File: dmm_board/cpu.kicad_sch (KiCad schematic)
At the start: 3 parts

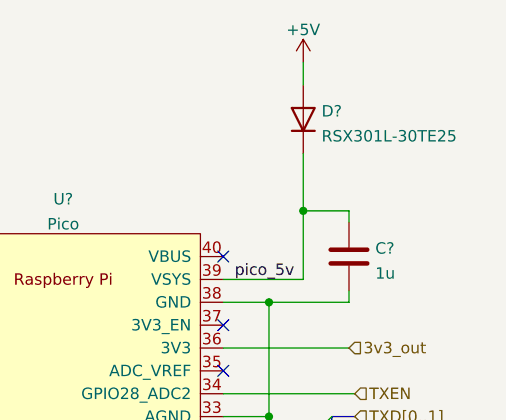
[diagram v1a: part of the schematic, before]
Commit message: more analog input work
need new amp for current -8 instead of -9 that
-8 is unity gain stable -9 is not
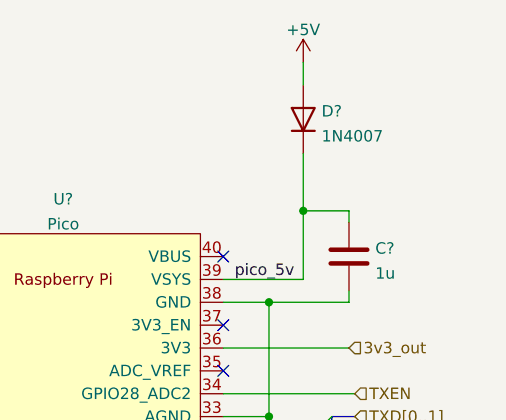
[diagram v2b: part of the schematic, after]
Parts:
- removed D?: RSX301L-30TE25, good_things:SOD-106, symbol Device:D
- added D?: 1N4007, Diode_THT:D_DO-41_SOD81_P7.62mm_Horizontal, symbol Device:D
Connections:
- net +5V: now also D?.2 (A)
- net pico_5v: now also D?.1 (K)
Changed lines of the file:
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@@
       (effects (font (size 1.27 1.27)) (justify right))
     )
-    (property "Value" "RSX301L-30TE25" (id 1) (at 121.412 37.4266 90)
+    (property "Value" "1N4007" (id 1) (at 121.412 37.4266 90)
       (effects (font (size 1.27 1.27)) (justify right))
     )
-    (property "Footprint" "good_things:SOD-106" (id 2) (at 119.38 35.56 0)
+    (property "Footprint" "Diode_THT:D_DO-41_SOD81_P7.62mm_Horizontal" (id 2) (at 119.38 35.56 0)
       (effects (font (size 1.27 1.27)) hide)
     )
